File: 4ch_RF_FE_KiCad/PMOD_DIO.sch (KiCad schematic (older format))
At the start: 34 parts, among them J2 PPTC062LJBN-RC, U10 SN74HCU04PWR, U7 PCA9548APW, U8 M24C02-FDW, U9 SN74LVC125APWR

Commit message: (+) starting layout
Signed-off-by: Gentile, John <johncgentile17@gmail.com>
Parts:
- J2: footprint digikey-footprints:PinHeader_2x6_P2.54mm_Vertical_SMD -> Connector_PinHeader_2.54mm:PinHeader_2x06_P2.54mm_Horizontal
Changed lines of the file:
@@
 F 0 "J2" H 3700 2303 60  0000 C CNN
 F 1 "PPTC062LJBN-RC" H 3700 2197 60  0000 C CNN
-F 2 "digikey-footprints:PinHeader_2x6_P2.54mm_Vertical_SMD" H 3900 1950 60  0001 L CNN
+F 2 "Connector_PinHeader_2.54mm:PinHeader_2x06_P2.54mm_Horizontal" H 3900 1950 60  0001 L CNN
 F 3 "https://media.digikey.com/pdf/Data%20Sheets/Sullins%20PDFs/Female_Headers.100_DS.pdf" H 3900 2050 60  0001 L CNN
 F 4 "S5520-ND" H 3900 2150 60  0001 L CNN "Digi-Key_PN"

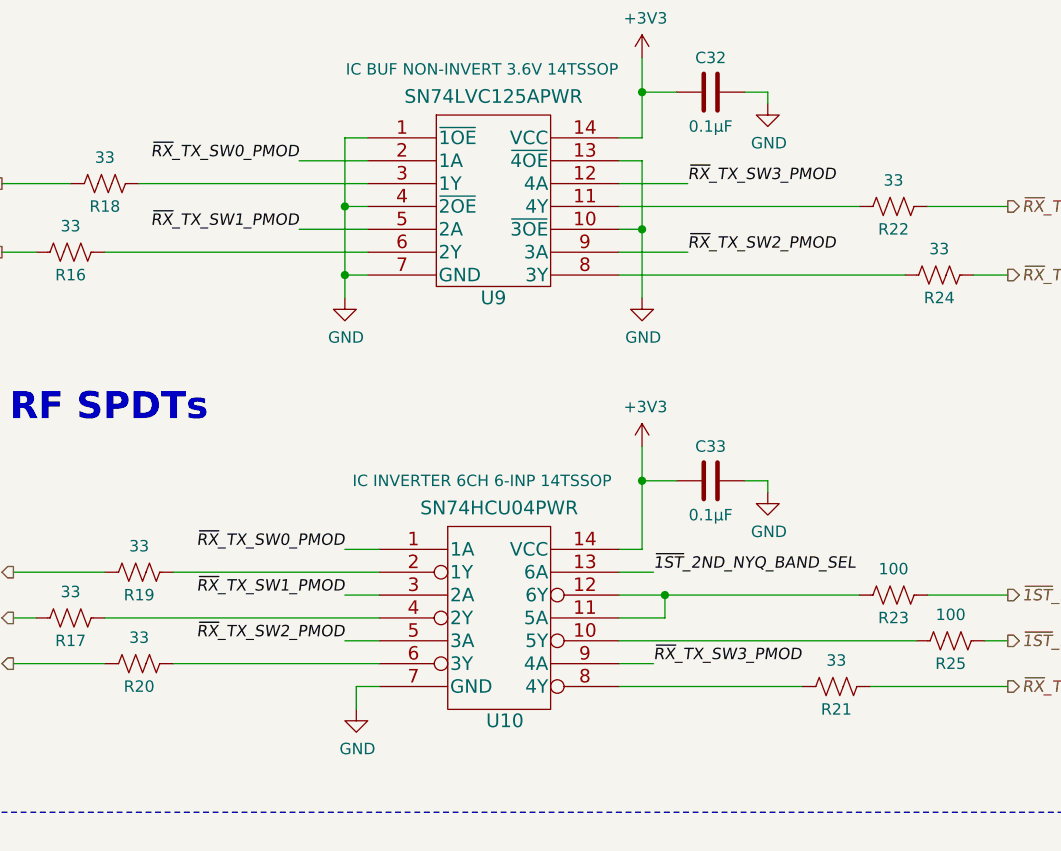
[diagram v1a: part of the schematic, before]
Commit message: (+) power & DIO layout & impedance calcs
Signed-off-by: Gentile, John <johncgentile17@gmail.com>
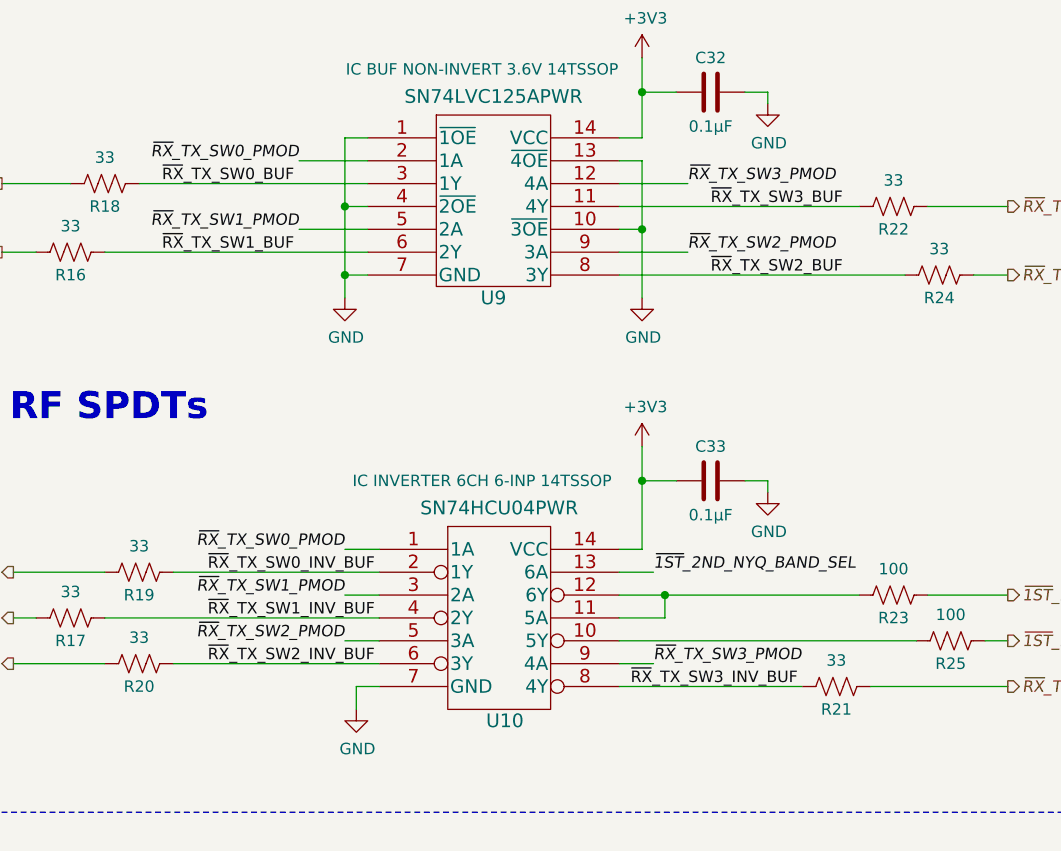
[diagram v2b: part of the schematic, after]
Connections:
- net ~RX~_TX_SW1_BUF: now reaches R16.1, U9.6 (2Y)
- net ~RX~_TX_SW3_BUF: now reaches R22.2, U9.11 (4Y)
- net ~RX~_TX_SW2_BUF: now reaches R24.2, U9.8 (3Y)
- net ~RX~_TX_SW3_INV_BUF: now reaches R21.2, U10.8 (4Y)
- net ~RX~_TX_SW0_INV_BUF: now reaches R19.1, U10.2 (1Y)
- net ~RX~_TX_SW1_INV_BUF: now reaches R17.1, U10.4 (2Y)
- net ~RX~_TX_SW2_INV_BUF: now reaches R20.1, U10.6 (3Y)
- net ~RX~_TX_SW0_BUF: now reaches R18.1, U9.3 (1Y)
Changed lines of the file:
@@
 	0    1    1    0
 $EndComp
+Text Label 10850 1500 0    50   ~ 0
+~RX~_TX_SW0_BUF
+Text Label 10850 1800 0    50   ~ 0
+~RX~_TX_SW1_BUF
+Text Label 13250 1600 0    50   ~ 0
+~RX~_TX_SW3_BUF
+Text Label 13250 1900 0    50   ~ 0
+~RX~_TX_SW2_BUF
+Text Label 11050 3200 0    50   ~ 0
+~RX~_TX_SW0_INV_BUF
+Text Label 11050 3400 0    50   ~ 0
+~RX~_TX_SW1_INV_BUF
+Text Label 11050 3600 0    50   ~ 0
+~RX~_TX_SW2_INV_BUF
+Text Label 12900 3700 0    50   ~ 0
+~RX~_TX_SW3_INV_BUF
 $EndSCHEMATC

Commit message: RF layout
Signed-off-by: Gentile, John <johncgentile17@gmail.com>
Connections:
- net EEPROM_SCL: now also RN3.1 (R1.1); no longer RN3.3 (R3.1)
- net EEPROM_SDA: now also RN3.2 (R2.1); no longer RN3.4 (R4.1)
- net GND: now also J2.7, U7.17 (SD6), U7.18 (SC6), U7.19 (SD7), U7.20 (SC7)
- net INA219_PWR_MON_SCL: now also RN3.3 (R3.1); no longer RN3.1 (R1.1)
- net INA219_PWR_MON_SDA: now also RN3.4 (R4.1); no longer RN3.2 (R2.1)
- net RF_CH0_ATTN_SCL: now also RN1.3 (R3.1); no longer RN1.1 (R1.1)
- net RF_CH0_ATTN_SDA: now also RN1.4 (R4.1); no longer RN1.2 (R2.1)
- net RF_CH1_ATTN_SCL: now also RN1.1 (R1.1); no longer RN1.3 (R3.1)
- net RF_CH1_ATTN_SDA: now also RN1.2 (R2.1); no longer RN1.4 (R4.1)
- net RF_CH2_ATTN_SCL: now also RN2.3 (R3.1); no longer RN2.1 (R1.1)
- net RF_CH2_ATTN_SDA: now also RN2.4 (R4.1); no longer RN2.2 (R2.1)
- net RF_CH3_ATTN_SCL: now also RN2.1 (R1.1); no longer RN2.3 (R3.1)
- net RF_CH3_ATTN_SDA: now also RN2.2 (R2.1); no longer RN2.4 (R4.1)
- no-connect marks 5 -> 0
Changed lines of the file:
@@
 Wire Wire Line
 	4700 1000 4800 1000
-Wire Wire Line
-	3200 6400 3300 6400
-Wire Wire Line
-	3300 6400 3300 6350
-Wire Wire Line
-	3200 6500 3400 6500
-Wire Wire Line
-	3200 6600 3500 6600
-Wire Wire Line
-	3500 6600 3500 6350
-Wire Wire Line
-	3600 6350 3600 6700
-Wire Wire Line
-	3600 6700 3200 6700
 Text HLabel 5750 6400 2    50   Output Italic 0
 RF_CH0_ATTN_SCL
@@
 Wire Wire Line
 	4600 5900 4250 5900
-Wire Wire Line
-	3950 6350 3950 6800
-Wire Wire Line
-	3950 6800 3200 6800
-Wire Wire Line
-	3200 6900 4050 6900
-Wire Wire Line
-	4050 6900 4050 6350
-Wire Wire Line
-	3200 7000 4150 7000
-Wire Wire Line
-	4150 7000 4150 6350
-Wire Wire Line
-	3200 7100 4250 7100
-Wire Wire Line
-	4250 7100 4250 6350
-Wire Wire Line
-	3200 7200 4600 7200
-Wire Wire Line
-	4600 7200 4600 6350
-Wire Wire Line
-	3200 7300 4700 7300
-Wire Wire Line
-	4700 7300 4700 6350
-Wire Wire Line
-	3200 7400 4800 7400
-Wire Wire Line
-	4800 7400 4800 6350
-Wire Wire Line
-	3200 7500 4900 7500
-Wire Wire Line
-	4900 7500 4900 6350
-Wire Wire Line
-	5750 6400 3300 6400
-Connection ~ 3300 6400
 Text HLabel 5750 6500 2    50   BiDi Italic 0
 RF_CH0_ATTN_SDA
-Wire Wire Line
-	3400 6500 3400 6350
-Wire Wire Line
-	3400 6500 5750 6500
-Connection ~ 3400 6500
 Text HLabel 5750 6600 2    50   Output Italic 0
 RF_CH1_ATTN_SCL
 Text HLabel 5750 6700 2    50   BiDi Italic 0
 RF_CH1_ATTN_SDA
-Wire Wire Line
-	5750 6600 3500 6600
-Connection ~ 3500 6600
-Wire Wire Line
-	3600 6700 5750 6700
-Connection ~ 3600 6700
 Text HLabel 5750 6800 2    50   Output Italic 0
 RF_CH2_ATTN_SCL
@@
 Text HLabel 5750 7100 2    50   BiDi Italic 0
 RF_CH3_ATTN_SDA
-Wire Wire Line
-	5750 6800 3950 6800
-Connection ~ 3950 6800
-Wire Wire Line
-	4050 6900 5750 6900
-Connection ~ 4050 6900
-Wire Wire Line
-	5750 7000 4150 7000
-Connection ~ 4150 7000
-Wire Wire Line
-	4250 7100 5750 7100
-Connection ~ 4250 7100
 Text Notes 6750 6800 0    50   Italic 0
 ADDR: 0x20
@@
 Text HLabel 5750 7200 2    50   Output Italic 0
 INA219_PWR_MON_SCL
-Wire Wire Line
-	5750 7200 4600 7200
-Connection ~ 4600 7200
 Text HLabel 5750 7300 2    50   BiDi Italic 0
 INA219_PWR_MON_SDA
-Wire Wire Line
-	5750 7300 4700 7300
-Connection ~ 4700 7300
 Wire Notes Line
 	5700 6300 5700 7150
@@
 Text Label 5800 7500 0    50   Italic 0
 EEPROM_SDA
-Wire Wire Line
-	4800 7400 5800 7400
-Connection ~ 4800 7400
-Wire Wire Line
-	5800 7500 4900 7500
-Connection ~ 4900 7500
 Text Notes 6750 7450 0    50   Italic 0
 ADDR: 0x50
@@
 Text Notes 1900 8100 0    50   Italic 10
 ADDR: 0x70
-NoConn ~ 3200 7600
-NoConn ~ 3200 7700
-NoConn ~ 3200 7800
-NoConn ~ 3200 7900
 Wire Notes Line
 	500  3900 7250 3900
-NoConn ~ 3500 1850
 Text Notes 7750 2550 0    118  ~ 24
 DIO Buffer & Inversion for RF SPDTs
@@
 Text Label 12900 3700 0    50   ~ 0
 ~RX~_TX_SW3_INV_BUF
+Wire Wire Line
+	3500 1850 3250 1850
+Wire Wire Line
+	3250 1850 3250 1950
+Connection ~ 3250 1950
+$Comp
+L power:GND #PWR0201
+U 1 1 5E870FEA
+P 3300 8000
+F 0 "#PWR0201" H 3300 7750 50  0001 C CNN
+F 1 "GND" H 3305 7827 50  0000 C CNN
+F 2 "" H 3300 8000 50  0001 C CNN
+F 3 "" H 3300 8000 50  0001 C CNN
+	1    3300 8000
+	1    0    0    -1
+$EndComp
+Wire Wire Line
+	3200 7600 3300 7600
+Wire Wire Line
+	3300 7600 3300 7700
+Wire Wire Line
+	3200 7700 3300 7700
+Connection ~ 3300 7700
+Wire Wire Line
+	3300 7700 3300 7800
+Wire Wire Line
+	3200 7800 3300 7800
+Connection ~ 3300 7800
+Wire Wire Line
+	3300 7800 3300 7900
+Wire Wire Line
+	3200 7900 3300 7900
+Connection ~ 3300 7900
+Wire Wire Line
+	3300 7900 3300 8000
+Wire Wire Line
+	3200 7500 4700 7500
+Wire Wire Line
+	3200 7400 4600 7400
+Wire Wire Line
+	3200 7300 4900 7300
+Wire Wire Line
+	3200 7200 4800 7200
+Wire Wire Line
+	4600 6350 4600 7400
+Connection ~ 4600 7400
+Wire Wire Line
+	4600 7400 5800 7400
+Wire Wire Line
+	4700 6350 4700 7500
+Connection ~ 4700 7500
+Wire Wire Line
+	4700 7500 5800 7500
+Wire Wire Line
+	4800 6350 4800 7200
+Connection ~ 4800 7200
+Wire Wire Line
+	4800 7200 5750 7200
+Wire Wire Line
+	4900 6350 4900 7300
+Connection ~ 4900 7300
+Wire Wire Line
+	4900 7300 5750 7300
+Wire Wire Line
+	3200 7100 4050 7100
+Wire Wire Line
+	3200 7000 3950 7000
+Wire Wire Line
+	3200 6800 4150 6800
+Wire Wire Line
+	3950 6350 3950 7000
+Connection ~ 3950 7000
+Wire Wire Line
+	3950 7000 5750 7000
+Wire Wire Line
+	4050 6350 4050 7100
+Connection ~ 4050 7100
+Wire Wire Line
+	4050 7100 5750 7100
+Wire Wire Line
+	4150 6350 4150 6800
+Connection ~ 4150 6800
+Wire Wire Line
+	4150 6800 5750 6800
+Wire Wire Line
+	4250 6350 4250 6900
+Wire Wire Line
+	3200 6900 4250 6900
+Connection ~ 4250 6900
+Wire Wire Line
+	4250 6900 5750 6900
+Wire Wire Line
+	3200 6700 3400 6700
+Wire Wire Line
+	3200 6600 3300 6600
+Wire Wire Line
+	3200 6500 3600 6500
+Wire Wire Line
+	3200 6400 3500 6400
+Wire Wire Line
+	3300 6350 3300 6600
+Connection ~ 3300 6600
+Wire Wire Line
+	3300 6600 5750 6600
+Wire Wire Line
+	3400 6350 3400 6700
+Connection ~ 3400 6700
+Wire Wire Line
+	3400 6700 5750 6700
+Wire Wire Line
+	3500 6350 3500 6400
+Connection ~ 3500 6400
+Wire Wire Line
+	3500 6400 5750 6400
+Wire Wire Line
+	3600 6350 3600 6500
+Connection ~ 3600 6500
+Wire Wire Line
+	3600 6500 5750 6500
 $EndSCHEMATC

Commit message: final layout
Signed-off-by: Gentile, John <johncgentile17@gmail.com>
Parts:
- added DS2: LTST-C190KGKT, digikey-footprints:LED_0603, symbol dk_LED-Indication-Discrete:LTST-C190KGKT
- added R31: 75, Resistor_SMD:R_0603_1608Metric_Pad1.05x0.95mm_HandSolder, symbol Device:R_US
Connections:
- net +3V3: now also DS2.2
- net GND: now also R31.2
- net RF_CH0_ATTN_SCL: now also RN2.1 (R1.1), U7.11 (SC3); no longer RN1.3 (R3.1), U7.5 (SC0)
- net RF_CH0_ATTN_SDA: now also RN2.2 (R2.1), U7.10 (SD3); no longer RN1.4 (R4.1), U7.4 (SD0)
- net RF_CH1_ATTN_SCL: now also RN2.3 (R3.1), U7.9 (SC2); no longer RN1.1 (R1.1), U7.7 (SC1)
- net RF_CH1_ATTN_SDA: now also RN2.4 (R4.1), U7.8 (SD2); no longer RN1.2 (R2.1), U7.6 (SD1)
- net RF_CH2_ATTN_SCL: now also RN1.1 (R1.1), U7.7 (SC1); no longer RN2.3 (R3.1), U7.9 (SC2)
- net RF_CH2_ATTN_SDA: now also RN1.2 (R2.1), U7.6 (SD1); no longer RN2.4 (R4.1), U7.8 (SD2)
- net RF_CH3_ATTN_SCL: now also RN1.3 (R3.1), U7.5 (SC0); no longer RN2.1 (R1.1), U7.11 (SC3)
- net RF_CH3_ATTN_SDA: now also RN1.4 (R4.1), U7.4 (SD0); no longer RN2.2 (R2.1), U7.10 (SD3)
- new net: DS2.1, R31.1
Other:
- note added: "PWR Good LED\nVf: 1.9V - 2.4V\nIF: 20 mA"
- moved on the sheet: C31, U8
